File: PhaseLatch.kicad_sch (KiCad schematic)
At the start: 102 parts, among them J1 CLK_IN, J2 NC, J3 I_IN, J4 Q_IN, J5 Databus, J6 Chip select, J7 Addressbus, J8 Signals, P1 Conn_02x10_Odd_Even, P2 Conn_02x10_Odd_Even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

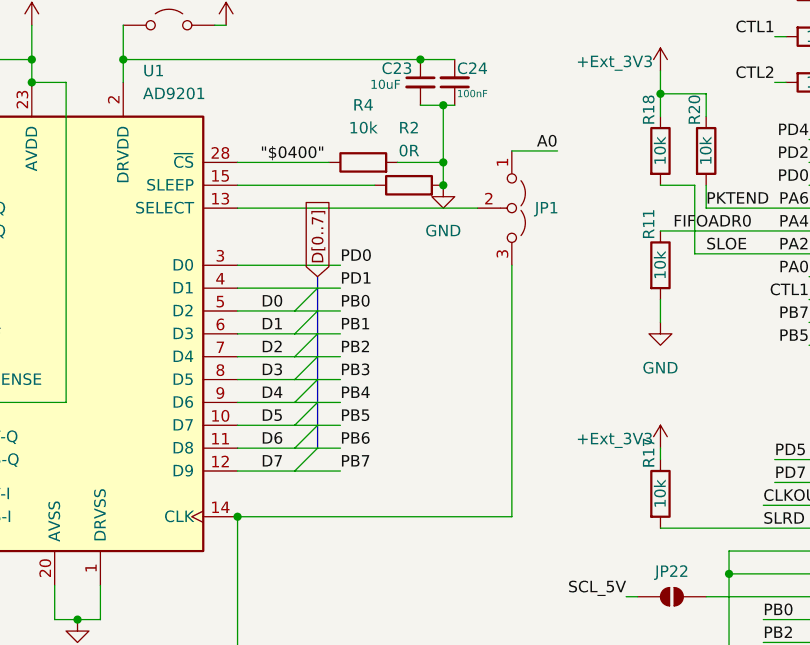
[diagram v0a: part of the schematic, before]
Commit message: Series termination, fork resistors
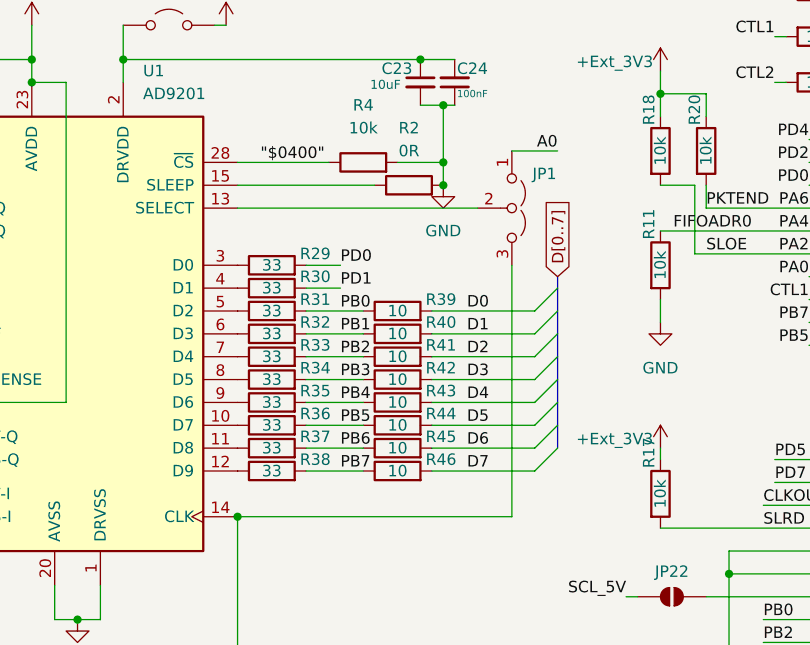
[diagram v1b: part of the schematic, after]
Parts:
- added R29, R30, R31, R32, R33, R34, R35, R36, R37, R38: 33, Resistor_SMD:R_0402_1005Metric, symbol Device:R
- added R39, R40, R41, R42, R43, R44, R45, R46: 10, Resistor_SMD:R_0402_1005Metric, symbol Device:R
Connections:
- net D0: now also R39.2; no longer P2.15 (Pin_15), U1.5 (D2)
- net D1: now also R40.2; no longer P2.16 (Pin_16), U1.6 (D3)
- net D2: now also R41.2; no longer P2.17 (Pin_17), U1.7 (D4)
- net D3: now also R42.2; no longer P2.18 (Pin_18), U1.8 (D5)
- net D4: now also R43.2; no longer P1.20 (Pin_20), U1.9 (D6)
- net D5: now also R44.2; no longer P1.19 (Pin_19), U1.10 (D7)
- net D6: now also R45.2; no longer P1.18 (Pin_18), U1.11 (D8)
- net D7: now also R46.2; no longer P1.17 (Pin_17), U1.12 (D9)
- net PD0: now also R29.2; no longer U1.3 (D0)
- net PD1: now also R30.2; no longer U1.4 (D1)
- new net: R37.1, U1.11 (D8)
- new net: R36.1, U1.10 (D7)
- new net: R30.1, U1.4 (D1)
- new net: R31.1, U1.5 (D2)
- new net: R32.1, U1.6 (D3)
- new net: R38.1, U1.12 (D9)
- new net: R29.1, U1.3 (D0)
- new net: R33.1, U1.7 (D4)
- new net: R34.1, U1.8 (D5)
- new net: R35.1, U1.9 (D6)
- new net PB0: P2.15 (Pin_15), R31.2, R39.1
- new net PB1: P2.16 (Pin_16), R32.2, R40.1
- new net PB2: P2.17 (Pin_17), R33.2, R41.1
- new net PB3: P2.18 (Pin_18), R34.2, R42.1
- new net PB4: P1.20 (Pin_20), R35.2, R43.1
- new net PB5: P1.19 (Pin_19), R36.2, R44.1
- new net PB6: P1.18 (Pin_18), R37.2, R45.1
- new net PB7: P1.17 (Pin_17), R38.2, R46.1
